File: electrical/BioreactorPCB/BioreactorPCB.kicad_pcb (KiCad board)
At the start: 2 copper layers, 90.7 x 84.9 mm, 90 parts, among them IC1 AL5809-20P1-7, IC2 VEML7700-TR, J1 61300311121, J10 USB_B, J11 Conn_01x06_Male, J12 Conn_02x03_Odd_Even, J13 PJ-202A, J14 Conn_01x05_Male, J15 Conn_01x06_Male, J16 Conn_01x06_Male, J2 61300311121, J3 Conn_01x05_Male, J4 Conn_01x06_Male, J5 OSTTC022162, J6 OSTTC022162, J7 OSTTC042162, J8 OSTTC042162, J9 OSTTC042162, Q1 2N3905, Q2 IRF540N, Q3 FQP47P06, Q4 TL2575HV-05IKV, U1 L293D, U2 FT232RL, U3 ATMEGA328P-AUR, U4 TCA39306DCUR, U5 ATmega328PB-M, Y1 16 mHz

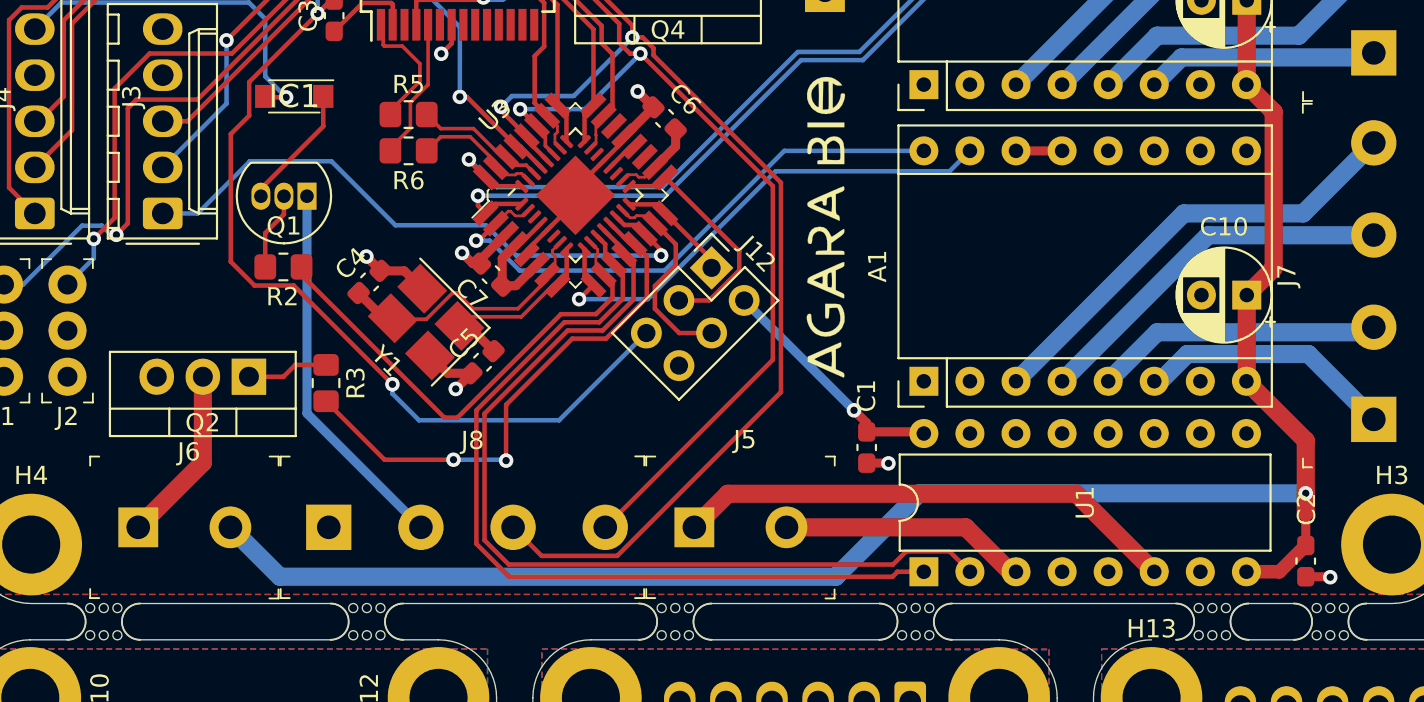
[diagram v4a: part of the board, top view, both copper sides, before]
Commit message: changed MOSFET to PFET and made the heater switched by a high-side switch
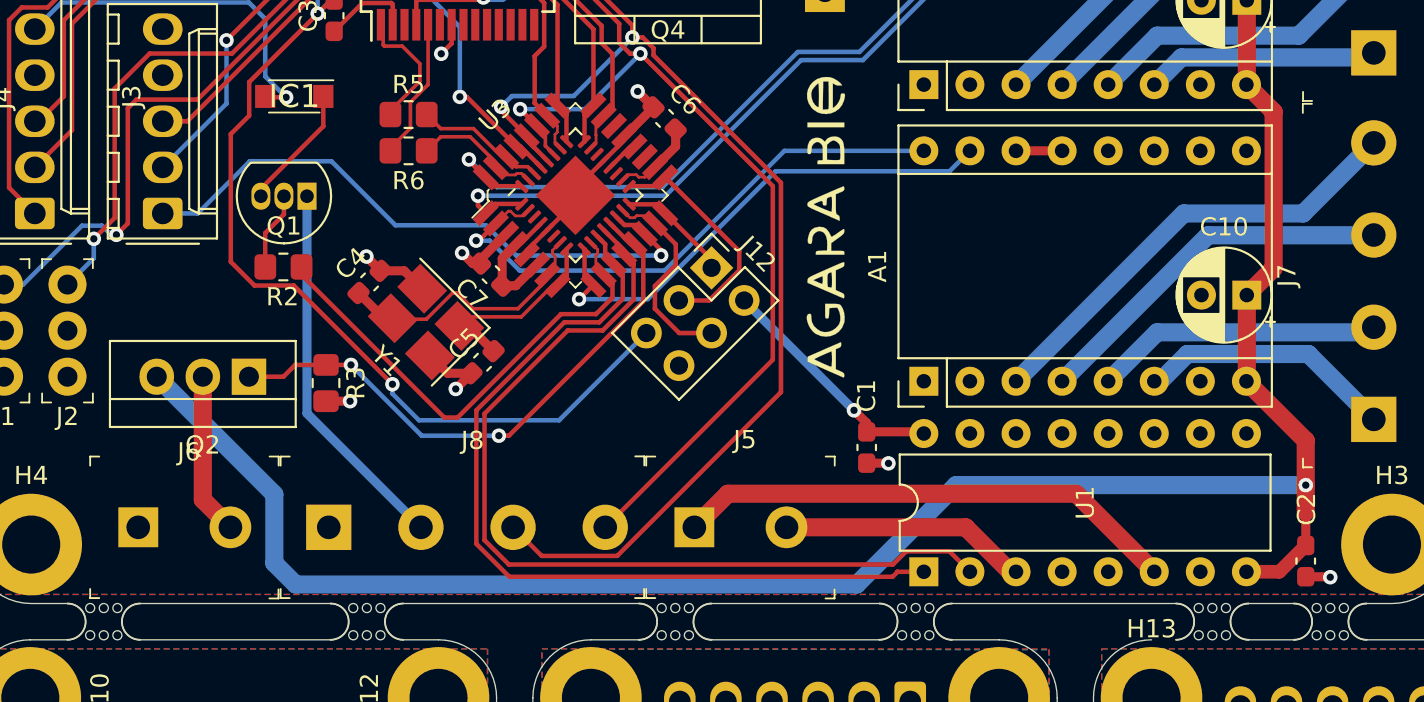
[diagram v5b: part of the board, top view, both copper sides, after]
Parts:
- Q2: value IRF540N -> IRF4905; footprint Package_TO_SOT_THT:TO-220-3_Vertical -> Package_TO_SOT_THT:TO-262-3_Vertical
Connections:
- J6 pad 1: Net-(J6-Pad1) -> GND
- J6 pad 2: +12V -> Net-(J6-Pad2)
- Q2 pad 1: Net-(Q2-Pad1) -> D9
- Q2 pad 2: Net-(J6-Pad1) -> Net-(J6-Pad2)
- Q2 pad 3: GND -> +12V
- R3 pad 1: Net-(Q2-Pad1) -> D9
- R3 pad 2: D9 -> GND
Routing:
- net +12V: track 151.9 -> 162.2 mm
- net Net-(J6-Pad1): track 9.77 -> 0.00 mm
- net Net-(J6-Pad2): track 0.00 -> 8.93 mm
- net Net-(Q2-Pad1): track 4.52 -> 0.00 mm
- net D9: track 29.4 -> 31.7 mm
- net XTAL-: track 11.1 -> 9.65 mm
- net XTAL+: track 15.0 -> 13.7 mm
- net GND: track 30.9 -> 32.0 mm, vias 10 -> 11

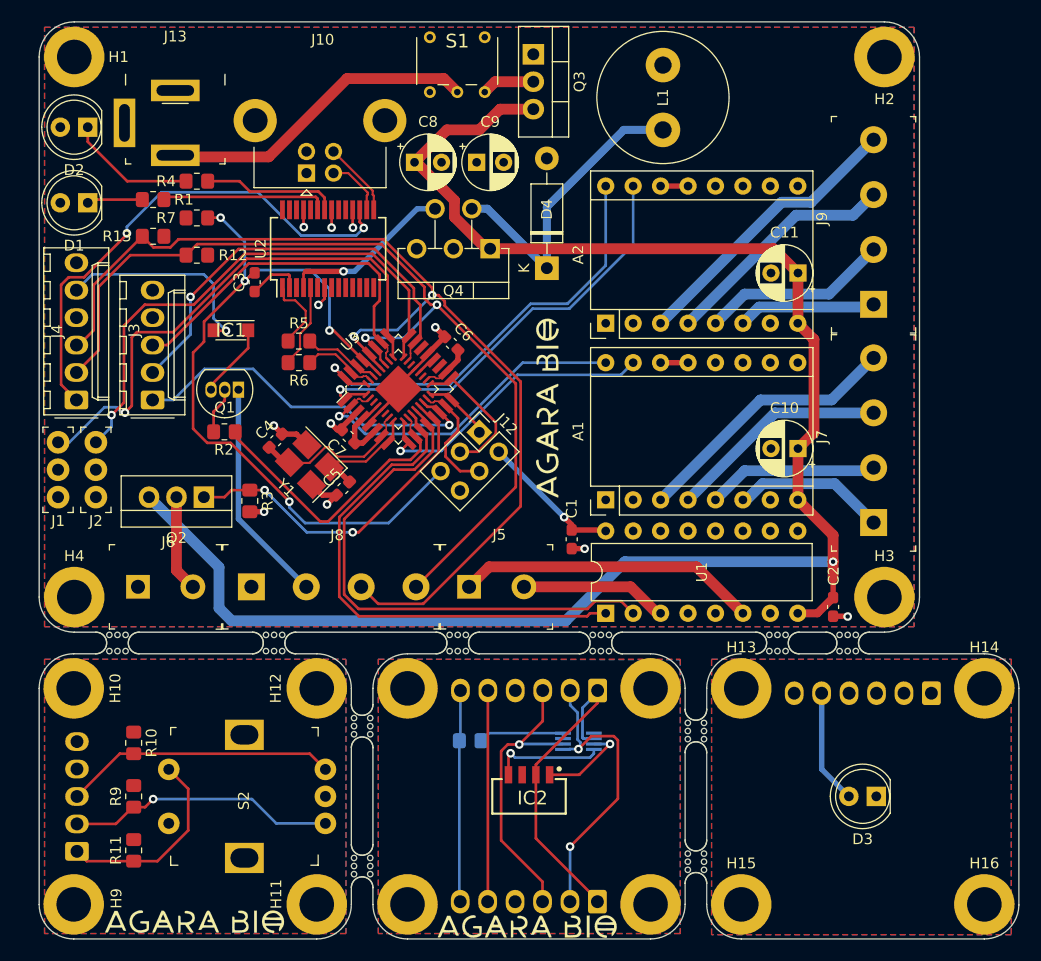
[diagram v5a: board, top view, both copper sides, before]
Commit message: NOW a 4-layer pCB with drastically improved routing
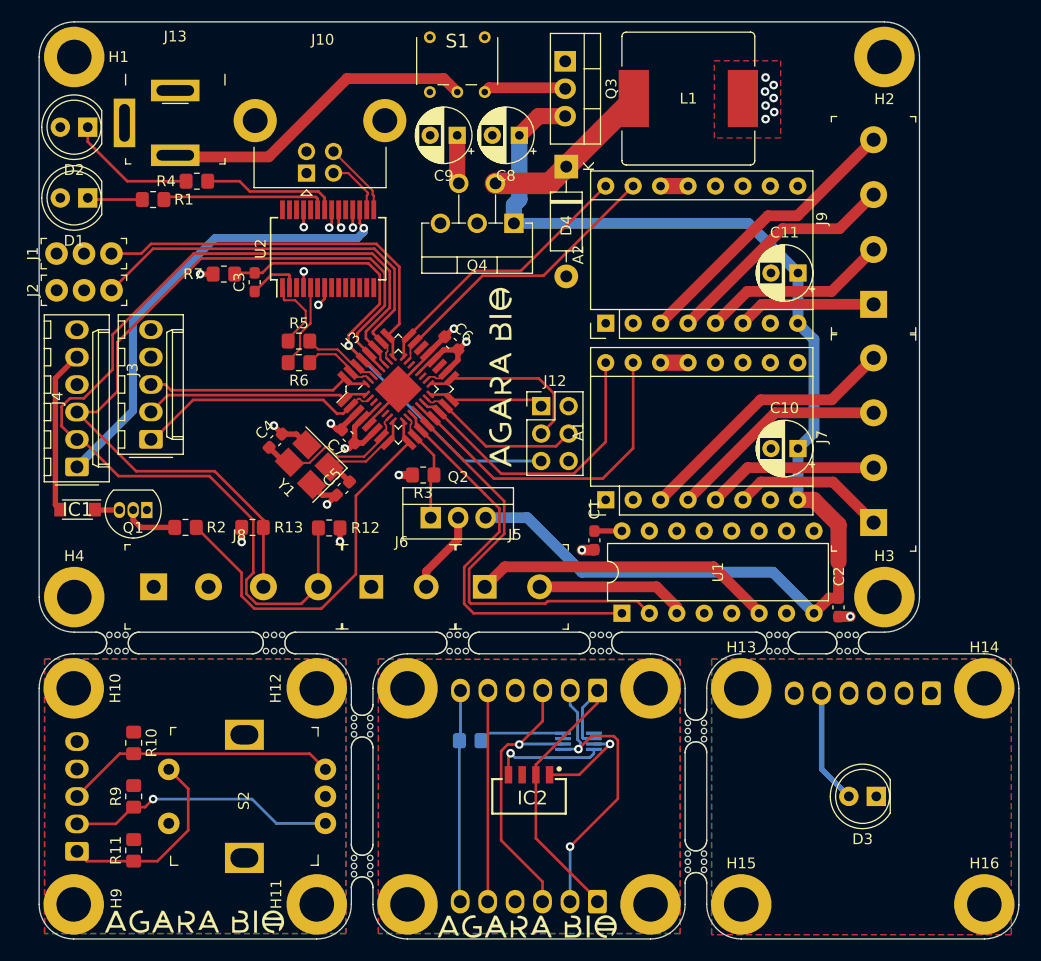
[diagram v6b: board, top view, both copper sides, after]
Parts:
- L1: footprint Inductor_THT:L_Radial_D12.0mm_P6.00mm_MuRATA_1900R -> Inductor_SMD:L_Bourns_SRR1210A
- moved R13 28.5 mm to (101.5, 84.3), turned to 180 degrees
- moved R12 28.1 mm to (108.6, 84.3)
- moved IC1 21.8 mm to (85.3, 82.7)
- moved J6 21.6 mm to (112.5, 89.8)
- moved Q2 21.1 mm to (118.0, 83.4), turned to 0 degrees
- moved J1 18.2 mm to (88.4, 59.0), turned to 180 degrees
- moved R3 16.2 mm to (117.3, 79.5), turned to 180 degrees
- moved J2 14.1 mm to (88.5, 62.4), turned to 180 degrees
- moved Q1 14.0 mm to (91.7, 82.7)
- moved C8 10.0 mm to (126.2, 48.0), turned to 180 degrees
- moved D4 9.57 mm to (130.6, 50.9), turned to -90 degrees
- moved R2 9.55 mm to (95.3, 84.3)
- moved J8 9.05 mm to (92.3, 89.8)
- moved J12 6.22 mm to (128.2, 73.1), turned to 0 degrees
- moved J4 6.20 mm to (85.2, 78.7)
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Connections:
- U3 pad 1: D3 -> ROT_A
- U3 pad 10: D6 -> D9
- U3 pad 13: D9 -> D5
- U3 pad 14: BUTTON -> D4
- U3 pad 2: D4 -> BUTTON
- U3 pad 23: ROT_A -> D3
- U3 pad 24: PH_OUT -> D2
- U3 pad 26: ROT_B -> PH_OUT
- U3 pad 32: D2 -> ROT_B
- U3 pad 9: D5 -> D6
- U5 pad 1: D3 -> ROT_A
- U5 pad 10: D6 -> D9
- U5 pad 13: D9 -> D5
- U5 pad 14: BUTTON -> D4
- U5 pad 2: D4 -> BUTTON
- U5 pad 23: ROT_A -> D3
- U5 pad 24: PH_OUT -> D2
- U5 pad 26: ROT_B -> PH_OUT
- U5 pad 32: D2 -> ROT_B
- U5 pad 9: D5 -> D6
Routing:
- net +12V: track 162.2 -> 112.2 mm, vias 1 -> 0
- net +5V: track 62.9 -> 32.0 mm, vias 2 -> 14
- net RESET: track 72.4 -> 48.0 mm, vias 4 -> 1
- net SCL: track 97.7 -> 75.8 mm, vias 2 -> 0
- net D9: track 31.7 -> 9.91 mm, vias 2 -> 0
- net ROT_A: track 39.3 -> 21.0 mm, vias 1 -> 0
- net D2: track 41.2 -> 26.1 mm, vias 1 -> 0
- net D3: track 41.5 -> 27.6 mm, vias 1 -> 0
- net TEMP_OUT: track 50.1 -> 36.9 mm, vias 1 -> 0
- net ROT_B: track 33.5 -> 20.8 mm
- net Net-(D4-Pad1): track 28.6 -> 16.0 mm
- net BUTTON: track 34.3 -> 23.1 mm, vias 1 -> 0
- net D6: track 26.1 -> 36.9 mm
- net D8: track 50.2 -> 39.7 mm
- net D7: track 47.5 -> 37.3 mm
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- added copper zone on In2.Cu, net +5V
- added copper zone on In1.Cu, net GND
- removed copper zone on B.Cu, net GND
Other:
- copper layers 2 -> 4

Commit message: +12V is now bottom copper plane
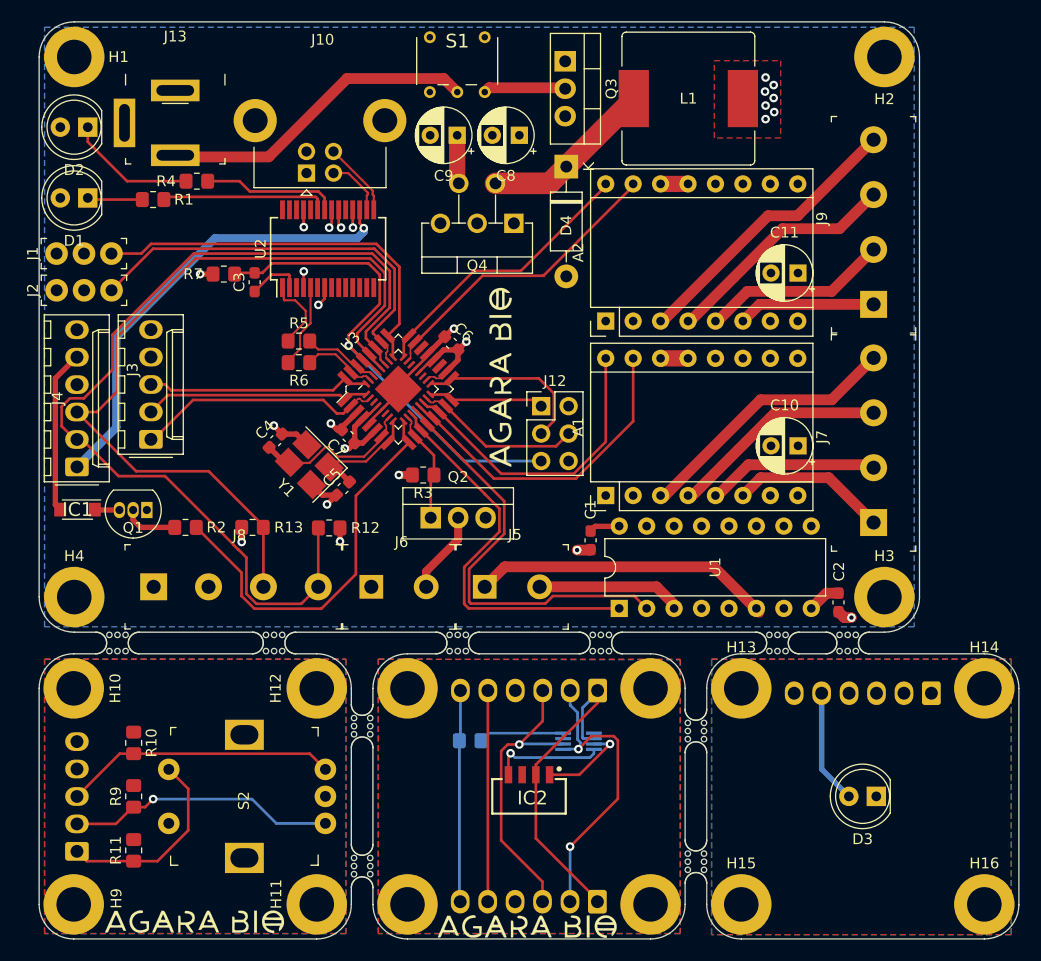
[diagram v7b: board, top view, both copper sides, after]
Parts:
- moved U1 0.51 mm to (135.4, 91.8)
- moved C2 0.45 mm to (155.8, 91.2)
- moved A1 0.40 mm to (134.2, 81.3)
- moved C1 0.35 mm to (132.8, 85.5)
- moved C10 0.25 mm to (152.0, 76.8)
- moved A2 0.20 mm to (134.2, 65.2)
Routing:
- net +12V: track 112.2 -> 3.11 mm
- net SDA: track 91.9 -> 88.3 mm
- net D5: track 31.5 -> 30.4 mm
- net MISO: track 10.7 -> 9.89 mm
- net Net-(J5-Pad2): track 14.0 -> 13.5 mm
- added copper zone on B.Cu, net +12V
